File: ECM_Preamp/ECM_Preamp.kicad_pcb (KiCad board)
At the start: 2 copper layers, 122.9 x 42.2 mm, 27 parts, among them J1 Conn_Coaxial, J2 XLR3, Q1 BF245C, SW1 SW_DIP_x02

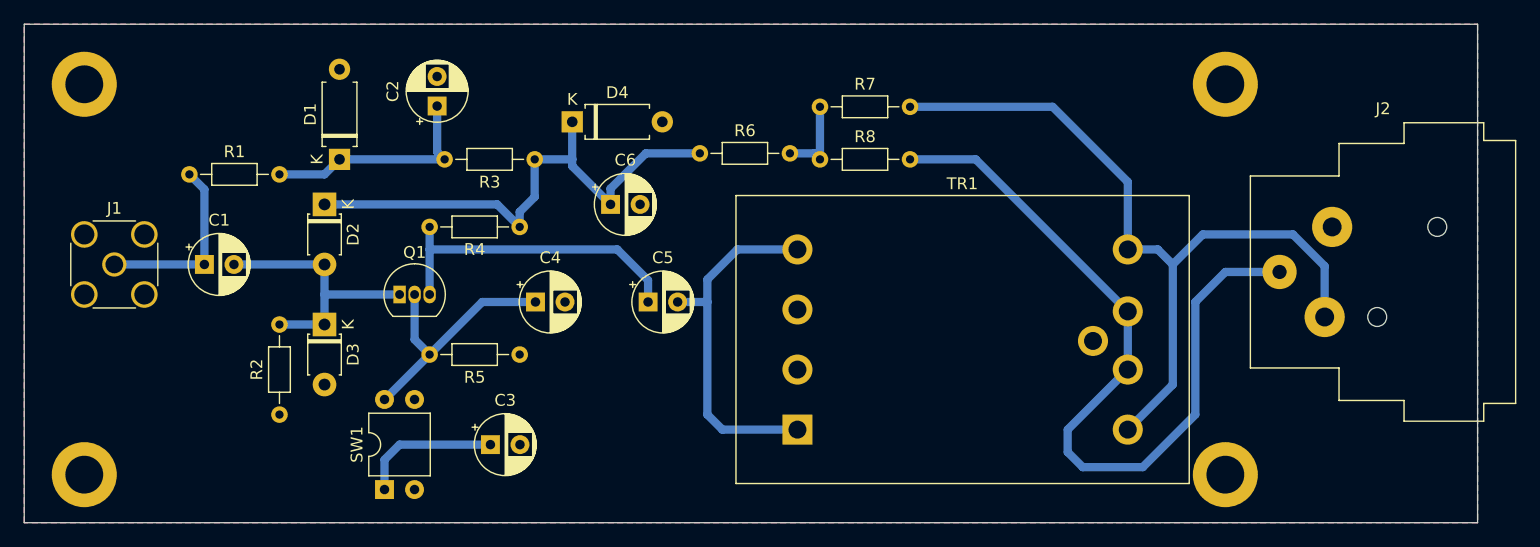
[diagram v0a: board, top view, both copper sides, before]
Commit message: sim updated, C_pol updated
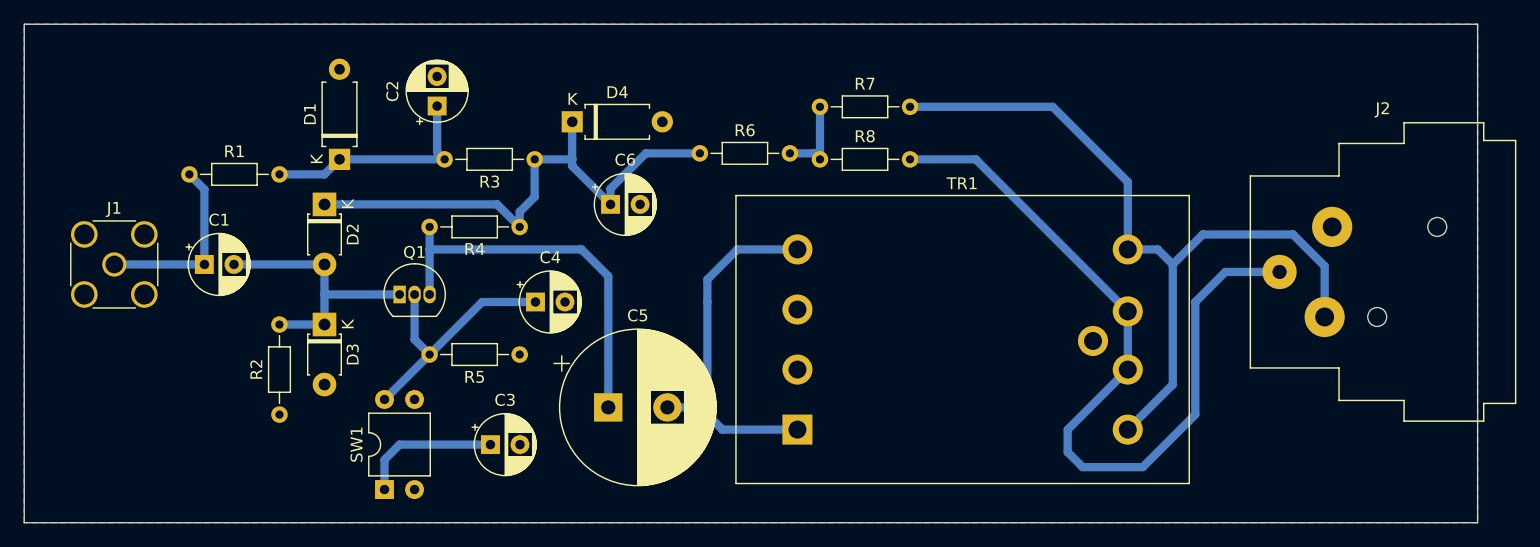
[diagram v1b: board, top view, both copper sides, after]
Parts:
- removed REF** (x4): MountingHole_3.2mm_M3_ISO14580_Pad, MountingHole:MountingHole_3.2mm_M3_ISO14580_Pad
- C5: value C_Polarized -> 1000u/35V; footprint Capacitor_THT:CP_Radial_D5.0mm_P2.50mm -> Capacitor_THT:CP_Radial_D13.0mm_P5.00mm
- moved C5 9.53 mm to (74.8, 57.8)
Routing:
- net Net-(C5-Pad1): track 27.1 -> 32.9 mm
- net Net-(C5-Pad2): track 30.8 -> 31.7 mm
